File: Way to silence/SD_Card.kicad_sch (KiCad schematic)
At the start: 7 parts, among them J1 SD Card Connector

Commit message: [DRC] Working on SD Sheet
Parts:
- removed C1: C, symbol Device:C
- added C1: C, symbol Way to silence:C
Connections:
- net GND: now also C1.2
- net 3.3V renamed +3.3V
- net +3.3V: now also C1.1
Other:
- moved on the sheet: J1, R1, R2, R3, R4, R5

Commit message: [UDPT] Changed pulled down to pulled up
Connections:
- net +3.3V: now also R1.1, R2.1, R3.1, R4.1, R5.1
- net GND: no longer R1.1, R2.1, R3.1, R4.1, R5.1
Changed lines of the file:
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@@
     (effects (font (size 1.27 1.27)) (justify right))
+  )
+  (symbol (lib_id "power:+3.3V") (at 30.48 44.45 90) (unit 1)
+    (in_bom yes) (on_board yes) (dnp no) (fields_autoplaced)
+    (property "Reference" "#PWR02" (at 34.29 44.45 0)
+      (effects (font (size 1.27 1.27)) hide)
+    )
+    (property "Value" "+3.3V" (at 26.67 44.45 90)
+      (effects (font (size 1.27 1.27)) (justify left))
+    )
+    (property "Footprint" "" (at 30.48 44.45 0)
+      (effects (font (size 1.27 1.27)) hide)
+    )
+    (property "Datasheet" "" (at 30.48 44.45 0)
+      (effects (font (size 1.27 1.27)) hide)
+    )
+    (pin "1")
+    (instances
+      (project "Way to silence"
+        (path "/9822a1be-a034-44c3-8530-56368958b215/7c0f88b3-e6fc-4dba-9c89-0d3e4a828f10"
+          (reference "#PWR02") (unit 1)
+        )
+      )
+    )
   )
   (symbol (lib_id "Way to silence:R") (at 39.37 44.45 0) (unit 1)
@@
         )
       )
-    )
-  )
-  (symbol (lib_id "power:GND") (at 30.48 44.45 270) (unit 1)
-    (in_bom yes) (on_board yes) (dnp no) (fields_autoplaced)
-    (property "Reference" "#PWR04" (at 24.13 44.45 0)
-      (effects (font (size 1.27 1.27)) hide)
-    )
-    (property "Value" "GND" (at 26.67 44.45 90)
-      (effects (font (size 1.27 1.27)) (justify right))
-    )
-    (property "Footprint" "" (at 30.48 44.45 0)
-      (effects (font (size 1.27 1.27)) hide)
-    )
-    (property "Datasheet" "" (at 30.48 44.45 0)
-      (effects (font (size 1.27 1.27)) hide)
-    )
-    (pin "1")
-    (instances
-      (project "Way to silence"
-        (path "/9822a1be-a034-44c3-8530-56368958b215/7c0f88b3-e6fc-4dba-9c89-0d3e4a828f10"
-          (reference "#PWR04") (unit 1)
-        )
-      )

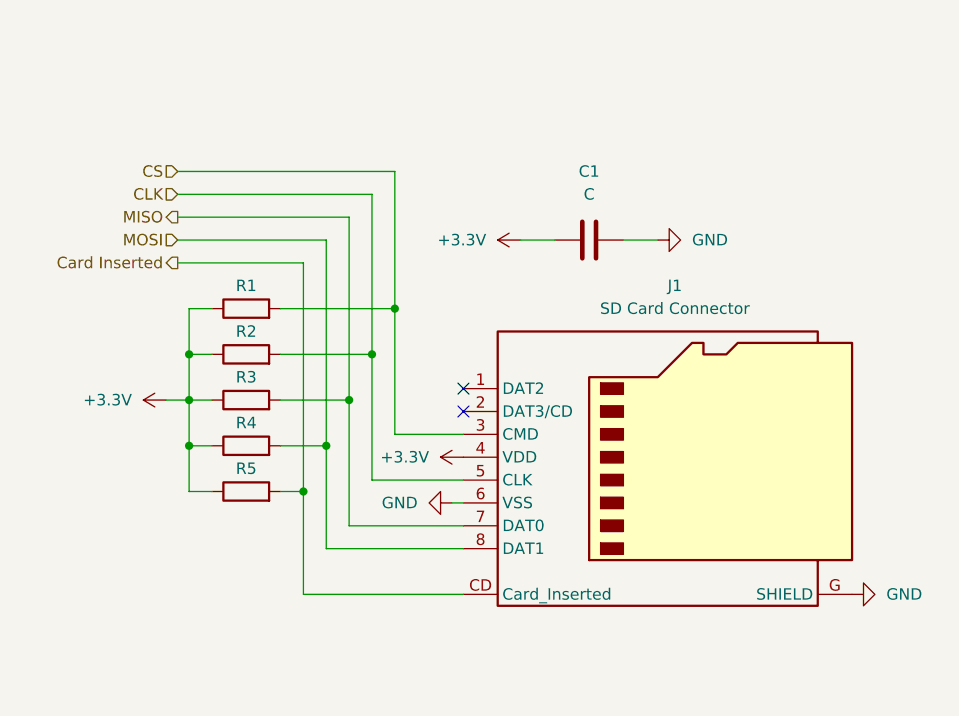
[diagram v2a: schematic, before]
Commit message: [ADD] USB C Connections
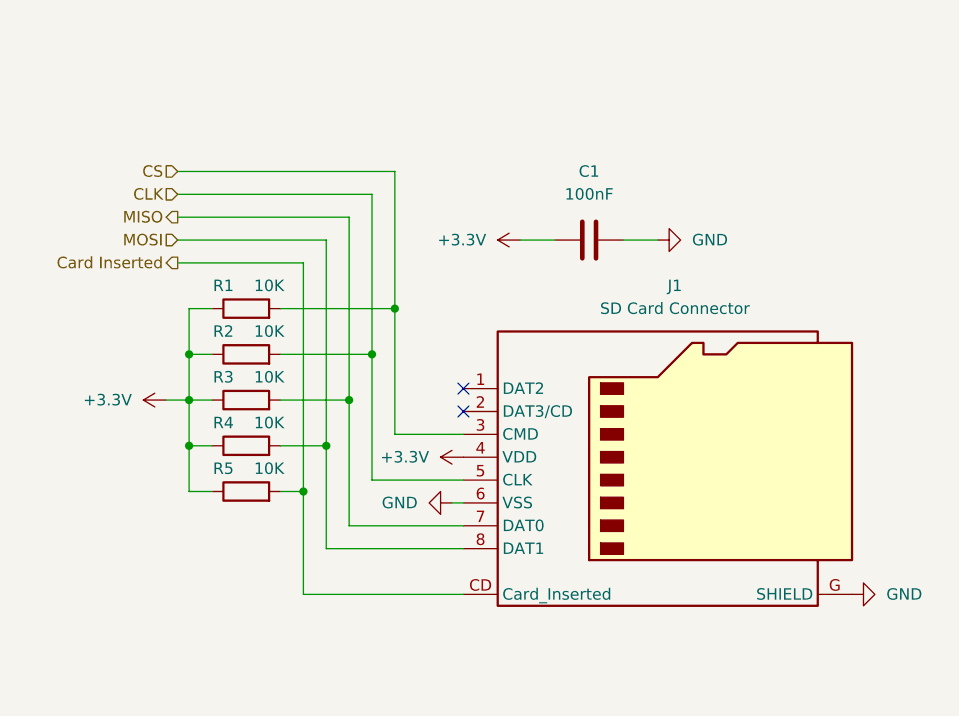
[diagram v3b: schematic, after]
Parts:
- C1: value C -> 100nF
- R1, R2, R3, R4, R5: value R -> 10K
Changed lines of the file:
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@@
   (symbol (lib_id "Way to silence:R") (at 39.37 44.45 0) (unit 1)
     (in_bom yes) (on_board yes) (dnp no)
-    (property "Reference" "R3" (at 39.37 41.91 0)
-      (effects (font (size 1.27 1.27)))
-    )
-    (property "Value" "R" (at 39.37 40.64 0)
-      (effects (font (size 1.27 1.27)) hide)
+    (property "Reference" "R3" (at 36.83 41.91 0)
+      (effects (font (size 1.27 1.27)))
+    )
+    (property "Value" "10K" (at 41.91 41.91 0)
+      (effects (font (size 1.27 1.27)))
     )
     (property "Footprint" "" (at 39.37 46.228 0)
@@
       (effects (font (size 1.27 1.27)))
     )
-    (property "Value" "C" (at 77.47 21.59 0)
+    (property "Value" "100nF" (at 77.47 21.59 0)
       (effects (font (size 1.27 1.27)))
     )
@@
   (symbol (lib_id "Way to silence:R") (at 39.37 39.37 0) (unit 1)
     (in_bom yes) (on_board yes) (dnp no)
-    (property "Reference" "R2" (at 39.37 36.83 0)
-      (effects (font (size 1.27 1.27)))
-    )
-    (property "Value" "R" (at 38.1 36.83 0)
-      (effects (font (size 1.27 1.27)) hide)
+    (property "Reference" "R2" (at 36.83 36.83 0)
+      (effects (font (size 1.27 1.27)))
+    )
+    (property "Value" "10K" (at 41.91 36.83 0)
+      (effects (font (size 1.27 1.27)))
     )
     (property "Footprint" "" (at 39.37 41.148 0)
@@
   (symbol (lib_id "Way to silence:R") (at 39.37 49.53 0) (unit 1)
     (in_bom yes) (on_board yes) (dnp no)
-    (property "Reference" "R4" (at 39.37 46.99 0)
-      (effects (font (size 1.27 1.27)))
-    )
-    (property "Value" "R" (at 39.37 45.72 0)
-      (effects (font (size 1.27 1.27)) hide)
+    (property "Reference" "R4" (at 36.83 46.99 0)
+      (effects (font (size 1.27 1.27)))
+    )
+    (property "Value" "10K" (at 41.91 46.99 0)
+      (effects (font (size 1.27 1.27)))
     )
     (property "Footprint" "" (at 39.37 51.308 0)
@@
   (symbol (lib_id "Way to silence:R") (at 39.37 54.61 0) (unit 1)
     (in_bom yes) (on_board yes) (dnp no)
-    (property "Reference" "R5" (at 39.37 52.07 0)
-      (effects (font (size 1.27 1.27)))
-    )
-    (property "Value" "R" (at 39.37 50.8 0)
-      (effects (font (size 1.27 1.27)) hide)
+    (property "Reference" "R5" (at 36.83 52.07 0)
+      (effects (font (size 1.27 1.27)))
+    )
+    (property "Value" "10K" (at 41.91 52.07 0)
+      (effects (font (size 1.27 1.27)))
     )
     (property "Footprint" "" (at 39.37 56.388 0)
@@
   (symbol (lib_id "Way to silence:R") (at 39.37 34.29 0) (unit 1)
     (in_bom yes) (on_board yes) (dnp no)
-    (property "Reference" "R1" (at 39.37 31.75 0)
-      (effects (font (size 1.27 1.27)))
-    )
-    (property "Value" "R" (at 38.1 31.75 0)
-      (effects (font (size 1.27 1.27)) hide)
+    (property "Reference" "R1" (at 36.83 31.75 0)
+      (effects (font (size 1.27 1.27)))
+    )
+    (property "Value" "10K" (at 41.91 31.75 0)
+      (effects (font (size 1.27 1.27)))
     )
     (property "Footprint" "" (at 39.37 36.068 0)

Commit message: [ADD] LSCS Parts and Footprints for BMS
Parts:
- C1: footprint (none) -> Way to silence:C_0603_1608Metric
- R1, R2, R3, R4, R5: footprint (none) -> Way to silence:R_0603_1608Metric
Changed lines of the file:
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@@
       (effects (font (size 1.27 1.27)))
     )
-    (property "Footprint" "" (at 39.37 46.228 0)
+    (property "Footprint" "Way to silence:R_0603_1608Metric" (at 39.37 46.228 0)
       (effects (font (size 1.27 1.27)) hide)
     )
@@
       (effects (font (size 1.27 1.27)))
     )
-    (property "Footprint" "" (at 81.28 25.7048 90)
+    (property "Footprint" "Way to silence:C_0603_1608Metric" (at 81.28 25.7048 90)
       (effects (font (size 1.27 1.27)) hide)
     )
@@
       (effects (font (size 1.27 1.27)))
     )
-    (property "Footprint" "" (at 39.37 41.148 0)
+    (property "Footprint" "Way to silence:R_0603_1608Metric" (at 39.37 41.148 0)
       (effects (font (size 1.27 1.27)) hide)
     )
@@
       (effects (font (size 1.27 1.27)))
     )
-    (property "Footprint" "" (at 39.37 51.308 0)
+    (property "Footprint" "Way to silence:R_0603_1608Metric" (at 39.37 51.308 0)
       (effects (font (size 1.27 1.27)) hide)
     )
@@
       (effects (font (size 1.27 1.27)))
     )
-    (property "Footprint" "" (at 39.37 56.388 0)
+    (property "Footprint" "Way to silence:R_0603_1608Metric" (at 39.37 56.388 0)
       (effects (font (size 1.27 1.27)) hide)
     )
@@
       (effects (font (size 1.27 1.27)))
     )
-    (property "Footprint" "" (at 39.37 36.068 0)
-      (effects (font (size 1.27 1.27)) hide)
-    )
+    (property "Footprint" "Way to silence:R_0603_1608Metric" (at 39.37 36.068 0)
+      (effects (font (size 1.27 1.27)) hide)
+    )

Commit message: [ADD] SD Card LCSC Refs
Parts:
- C1: LCSC (none) -> C14663
- R1, R2, R3, R4, R5: LCSC (none) -> C25804
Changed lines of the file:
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@@
+      (effects (font (size 1.27 1.27)) hide)
+    )
+    (property "LCSC" "C25804" (at 39.37 44.45 0)
       (effects (font (size 1.27 1.27)) hide)
     )
@@
     )
     (property "Datasheet" "~" (at 77.47 26.67 90)
+      (effects (font (size 1.27 1.27)) hide)
+    )
+    (property "LCSC" "C14663" (at 77.47 26.67 0)
       (effects (font (size 1.27 1.27)) hide)
     )
@@
       (effects (font (size 1.27 1.27)) hide)
     )
+    (property "LCSC" "C25804" (at 39.37 39.37 0)
+      (effects (font (size 1.27 1.27)) hide)
+    )
     (pin "1")
     (pin "2")
@@
       (effects (font (size 1.27 1.27)) hide)
     )
+    (property "LCSC" "C25804" (at 39.37 49.53 0)
+      (effects (font (size 1.27 1.27)) hide)
+    )
     (pin "1")
     (pin "2")
@@
     )
     (property "Datasheet" "~" (at 39.37 54.61 90)
+      (effects (font (size 1.27 1.27)) hide)
+    )
+    (property "LCSC" "C25804" (at 39.37 54.61 0)
       (effects (font (size 1.27 1.27)) hide)
     )
@@
       (effects (font (size 1.27 1.27)) hide)
     )
+    (property "LCSC" "C25804" (at 39.37 34.29 0)
+      (effects (font (size 1.27 1.27)) hide)
+    )

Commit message: [ADD] Shematics files settings
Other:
- title: (none) -> SD Card 
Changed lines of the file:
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@@
 (kicad_sch (version 20230121) (generator eeschema)
-  (paper "A4")
+  (paper "A5")
+  (title_block
+    (title "SD Card ")
+    (date "2023-10-10")
+    (rev "1.0")
+  )
   (junction (at 48.26 49.53) (diameter 0) (color 0 0 0 0)
   )

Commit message: [ADD] First design fixes
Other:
- note added: "CMD vers MOSI au lieu de DAT1 vers MOSI DAT3 vers CS au lieu de CMD vers CS"
- note added: "CS"
- note added: "MOSI"
- note added: "NC"
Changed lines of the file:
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@@
     (stroke (width 0) (type default))
+  )
+  (arc (start 43.18 34.29) (mid 55.8909 35.4701) (end 63.5 45.72)
+    (stroke (width 0) (type default))
+    (fill (type none))
+  )
+  (arc (start 48.26 49.53) (mid 55.6692 46.3653) (end 63.5 48.26)
+    (stroke (width 0) (type default))
+    (fill (type none))
+  )
+  (arc (start 54.61 29.21) (mid 56.515 28.4209) (end 58.42 29.21)
+    (stroke (width 0) (type default))
+    (fill (type none))
+  )
+  (arc (start 34.29 19.05) (mid 43.2912 24.0122) (end 43.18 34.29)
+    (stroke (width 0) (type default))
+    (fill (type none))
+  )
+  (rectangle (start 54.61 59.69) (end 54.61 62.23)
+    (stroke (width 0) (type default))
+    (fill (type none))
+  )
+  (arc (start 44.45 30.48) (mid 44.9019 33.655) (end 44.45 36.83)
+    (stroke (width 0) (type default))
+    (fill (type none))
+  )
+  (text "CMD vers MOSI au lieu de DAT1 vers MOSI\nDAT3 vers CS au lieu de CMD vers CS"
+    (at 24.13 17.78 0)
+    (effects (font (size 1.27 1.27) (color 255 0 34 1)) (justify left bottom))
+  )
+  (text "NC" (at 72.39 62.23 0)
+    (effects (font (size 1.27 1.27)) (justify left bottom))
+  )
+  (text "CS" (at 59.69 46.99 0)
+    (effects (font (size 1.27 1.27)) (justify left bottom))
+  )
+  (text "MOSI" (at 72.39 49.53 0)
+    (effects (font (size 1.27 1.27)) (justify left bottom))
   )
   (hierarchical_label "MOSI" (shape input) (at 31.75 26.67 180) (fields_autoplaced)

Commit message: [UDPT] Schematics from testings
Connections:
- net CLK: now also R3.2; no longer R2.2
- net CS: now also J1.2 (DAT3/CD); no longer J1.3 (CMD)
- net MISO: now also R4.2; no longer R3.2
- net MOSI: now also J1.3 (CMD), R2.2; no longer J1.8 (DAT1), R4.2
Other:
- note removed: "CS"
- note removed: "MOSI"
- note removed: "NC"
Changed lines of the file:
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@@
     (rev "1.0")
-  )
-  (junction (at 48.26 49.53) (diameter 0) (color 0 0 0 0)
-  )
-  (junction (at 50.8 44.45) (diameter 0) (color 0 0 0 0)
   )
   (junction (at 45.72 54.61) (diameter 0) (color 0 0 0 0)
@@
   (junction (at 33.02 44.45) (diameter 0) (color 0 0 0 0)
   )
+  (junction (at 48.26 49.53) (diameter 0) (color 0 0 0 0)
+  )
+  (junction (at 50.8 44.45) (diameter 0) (color 0 0 0 0)
+  )
   (junction (at 55.88 34.29) (diameter 0) (color 0 0 0 0)
+  )
+  (junction (at 33.02 49.53) (diameter 0) (color 0 0 0 0)
   )
   (junction (at 53.34 39.37) (diameter 0) (color 0 0 0 0)
   )
-  (junction (at 33.02 49.53) (diameter 0) (color 0 0 0 0)
-  )
-  (no_connect (at 63.5 45.72))
+  (no_connect (at 63.5 60.96))
   (no_connect (at 63.5 43.18))
   (wire (pts (xy 45.72 66.04) (xy 63.5 66.04))
     (stroke (width 0) (type default))
   )
-  (wire (pts (xy 53.34 21.59) (xy 31.75 21.59))
-    (stroke (width 0) (type default))
-  )
-  (wire (pts (xy 50.8 44.45) (xy 50.8 58.42))
-    (stroke (width 0) (type default))
-  )
-  (wire (pts (xy 43.18 44.45) (xy 50.8 44.45))
-    (stroke (width 0) (type default))
-  )
-  (wire (pts (xy 53.34 21.59) (xy 53.34 39.37))
-    (stroke (width 0) (type default))
-  )
-  (wire (pts (xy 48.26 26.67) (xy 48.26 49.53))
+  (wire (pts (xy 50.8 24.13) (xy 31.75 24.13))
     (stroke (width 0) (type default))
   )
@@
     (stroke (width 0) (type default))
   )
-  (wire (pts (xy 43.18 39.37) (xy 53.34 39.37))
+  (wire (pts (xy 53.34 39.37) (xy 53.34 48.26))
     (stroke (width 0) (type default))
   )
@@
     (stroke (width 0) (type default))
   )
-  (wire (pts (xy 55.88 19.05) (xy 55.88 34.29))
-    (stroke (width 0) (type default))
-  )
-  (wire (pts (xy 63.5 53.34) (xy 53.34 53.34))
+  (wire (pts (xy 63.5 53.34) (xy 50.8 53.34))
     (stroke (width 0) (type default))
   )
   (wire (pts (xy 33.02 39.37) (xy 33.02 34.29))
+    (stroke (width 0) (type default))
+  )
+  (wire (pts (xy 55.88 19.05) (xy 55.88 34.29))
     (stroke (width 0) (type default))
   )
@@
     (stroke (width 0) (type default))
   )
+  (wire (pts (xy 55.88 34.29) (xy 55.88 45.72))
+    (stroke (width 0) (type default))
+  )
   (wire (pts (xy 33.02 44.45) (xy 35.56 44.45))
+    (stroke (width 0) (type default))
+  )
+  (wire (pts (xy 43.18 44.45) (xy 50.8 44.45))
+    (stroke (width 0) (type default))
+  )
+  (wire (pts (xy 31.75 21.59) (xy 53.34 21.59))
     (stroke (width 0) (type default))
   )
@@
     (stroke (width 0) (type default))
   )
-  (wire (pts (xy 55.88 34.29) (xy 55.88 48.26))
+  (wire (pts (xy 43.18 39.37) (xy 53.34 39.37))
+    (stroke (width 0) (type default))
+  )
+  (wire (pts (xy 53.34 21.59) (xy 53.34 39.37))
+    (stroke (width 0) (type default))
+  )
+  (wire (pts (xy 31.75 19.05) (xy 55.88 19.05))
     (stroke (width 0) (type default))
   )
@@
     (stroke (width 0) (type default))
   )
-  (wire (pts (xy 63.5 48.26) (xy 55.88 48.26))
+  (wire (pts (xy 63.5 48.26) (xy 53.34 48.26))
     (stroke (width 0) (type default))
   )
-  (wire (pts (xy 50.8 24.13) (xy 50.8 44.45))
+  (wire (pts (xy 48.26 26.67) (xy 48.26 49.53))
     (stroke (width 0) (type default))
   )
   (wire (pts (xy 62.23 55.88) (xy 63.5 55.88))
-    (stroke (width 0) (type default))
-  )
-  (wire (pts (xy 31.75 26.67) (xy 48.26 26.67))
     (stroke (width 0) (type default))
   )
@@
   )
   (wire (pts (xy 30.48 44.45) (xy 33.02 44.45))
-    (stroke (width 0) (type default))
-  )
-  (wire (pts (xy 43.18 34.29) (xy 55.88 34.29))
     (stroke (width 0) (type default))
   )
@@
     (stroke (width 0) (type default))
   )
-  (wire (pts (xy 63.5 60.96) (xy 48.26 60.96))
+  (wire (pts (xy 55.88 45.72) (xy 63.5 45.72))
     (stroke (width 0) (type default))
   )
-  (wire (pts (xy 31.75 24.13) (xy 50.8 24.13))
+  (wire (pts (xy 31.75 26.67) (xy 48.26 26.67))
     (stroke (width 0) (type default))
   )
-  (wire (pts (xy 53.34 39.37) (xy 53.34 53.34))
+  (wire (pts (xy 50.8 44.45) (xy 50.8 53.34))
     (stroke (width 0) (type default))
   )
-  (wire (pts (xy 50.8 58.42) (xy 63.5 58.42))
+  (wire (pts (xy 48.26 49.53) (xy 48.26 58.42))
     (stroke (width 0) (type default))
   )
-  (wire (pts (xy 55.88 19.05) (xy 31.75 19.05))
+  (wire (pts (xy 50.8 24.13) (xy 50.8 44.45))
+    (stroke (width 0) (type default))
+  )
+  (wire (pts (xy 48.26 58.42) (xy 63.5 58.42))
     (stroke (width 0) (type default))
   )
@@
     (stroke (width 0) (type default))
   )
-  (wire (pts (xy 48.26 49.53) (xy 48.26 60.96))
+  (wire (pts (xy 43.18 34.29) (xy 55.88 34.29))
     (stroke (width 0) (type default))
   )
@@
     (stroke (width 0) (type default))
   )
-  (arc (start 43.18 34.29) (mid 55.8909 35.4701) (end 63.5 45.72)
-    (stroke (width 0) (type default))
-    (fill (type none))
-  )
-  (arc (start 48.26 49.53) (mid 55.6692 46.3653) (end 63.5 48.26)
-    (stroke (width 0) (type default))
-    (fill (type none))
-  )
-  (arc (start 54.61 29.21) (mid 56.515 28.4209) (end 58.42 29.21)
-    (stroke (width 0) (type default))
-    (fill (type none))
-  )
-  (arc (start 34.29 19.05) (mid 43.2912 24.0122) (end 43.18 34.29)
-    (stroke (width 0) (type default))
-    (fill (type none))
-  )
-  (rectangle (start 54.61 59.69) (end 54.61 62.23)
-    (stroke (width 0) (type default))
-    (fill (type none))
-  )
-  (arc (start 44.45 30.48) (mid 44.9019 33.655) (end 44.45 36.83)
-    (stroke (width 0) (type default))
-    (fill (type none))
-  )
   (text "CMD vers MOSI au lieu de DAT1 vers MOSI\nDAT3 vers CS au lieu de CMD vers CS"
-    (at 24.13 17.78 0)
+    (at 22.86 6.35 0)
     (effects (font (size 1.27 1.27) (color 255 0 34 1)) (justify left bottom))
   )
-  (text "NC" (at 72.39 62.23 0)
-    (effects (font (size 1.27 1.27)) (justify left bottom))
-  )
-  (text "CS" (at 59.69 46.99 0)
-    (effects (font (size 1.27 1.27)) (justify left bottom))
-  )
-  (text "MOSI" (at 72.39 49.53 0)
-    (effects (font (size 1.27 1.27)) (justify left bottom))
-  )
-  (hierarchical_label "MOSI" (shape input) (at 31.75 26.67 180) (fields_autoplaced)
+  (hierarchical_label "MOSI" (shape input) (at 31.75 21.59 180) (fields_autoplaced)
     (effects (font (size 1.27 1.27)) (justify right))
   )
@@
     (effects (font (size 1.27 1.27)) (justify right))
   )
-  (hierarchical_label "CLK" (shape input) (at 31.75 21.59 180) (fields_autoplaced)
+  (hierarchical_label "CLK" (shape input) (at 31.75 24.13 180) (fields_autoplaced)
     (effects (font (size 1.27 1.27)) (justify right))
   )
-  (hierarchical_label "MISO" (shape output) (at 31.75 24.13 180) (fields_autoplaced)
+  (hierarchical_label "MISO" (shape output) (at 31.75 26.67 180) (fields_autoplaced)
     (effects (font (size 1.27 1.27)) (justify right))
   )
